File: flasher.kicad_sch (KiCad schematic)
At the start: 22 parts, among them Q2 SS8050_C2150, Q3 SS8050_C2150, U5 CH343G

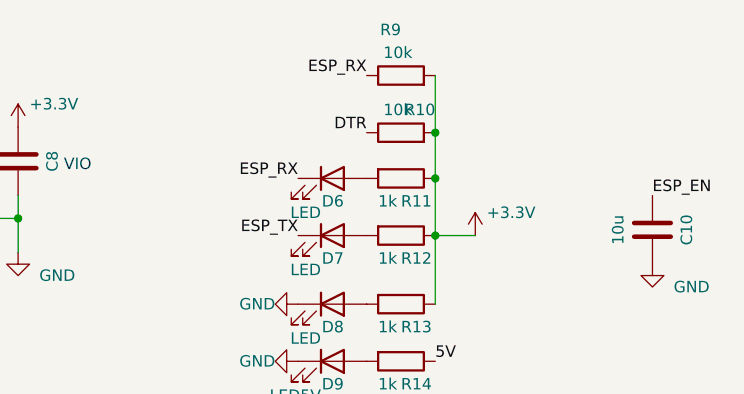
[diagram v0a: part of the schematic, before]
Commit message: changed footprints
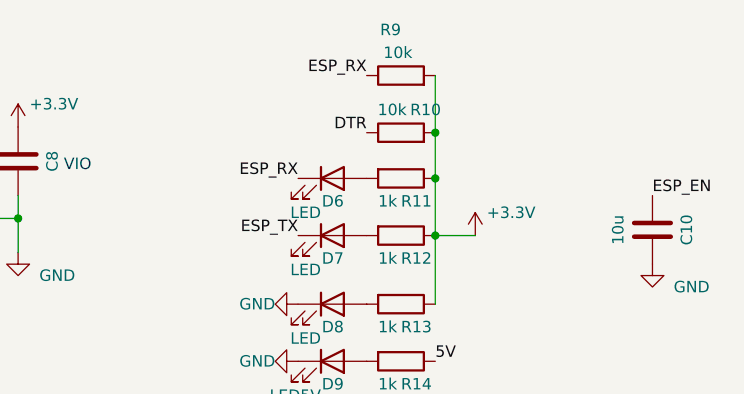
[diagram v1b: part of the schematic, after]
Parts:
- R10, R11, R12, R13, R14, R5, R6, R7, R8, R9: footprint Resistor_SMD:R_0402_1005Metric -> Resistor_SMD:R_1206_3216Metric
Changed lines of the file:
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@@
       (effects (font (size 1.27 1.27)) (justify left))
     )
-    (property "Footprint" "Resistor_SMD:R_0402_1005Metric" (at 132.715 38.862 90)
+    (property "Footprint" "Resistor_SMD:R_1206_3216Metric" (at 132.715 38.862 90)
       (effects (font (size 1.27 1.27)) hide)
     )
@@
       (effects (font (size 1.27 1.27)) (justify left))
     )
-    (property "Footprint" "Resistor_SMD:R_0402_1005Metric" (at 132.715 24.638 90)
+    (property "Footprint" "Resistor_SMD:R_1206_3216Metric" (at 132.715 24.638 90)
       (effects (font (size 1.27 1.27)) hide)
     )
@@
       (effects (font (size 1.27 1.27)) (justify left))
     )
-    (property "Footprint" "Resistor_SMD:R_0402_1005Metric" (at 132.715 46.482 90)
+    (property "Footprint" "Resistor_SMD:R_1206_3216Metric" (at 132.715 46.482 90)
       (effects (font (size 1.27 1.27)) hide)
     )
@@
   (symbol (lib_id "Device:R") (at 132.715 29.21 90) (unit 1)
     (in_bom yes) (on_board yes) (dnp no)
-    (property "Reference" "R10" (at 136.525 26.67 90)
-      (effects (font (size 1.27 1.27)) (justify left))
-    )
-    (property "Value" "10k" (at 133.985 26.67 90)
-      (effects (font (size 1.27 1.27)) (justify left))
-    )
-    (property "Footprint" "Resistor_SMD:R_0402_1005Metric" (at 132.715 30.988 90)
+    (property "Reference" "R10" (at 137.16 26.67 90)
+      (effects (font (size 1.27 1.27)) (justify left))
+    )
+    (property "Value" "10k" (at 133.35 26.67 90)
+      (effects (font (size 1.27 1.27)) (justify left))
+    )
+    (property "Footprint" "Resistor_SMD:R_1206_3216Metric" (at 132.715 30.988 90)
       (effects (font (size 1.27 1.27)) hide)
     )
@@
       (effects (font (size 1.27 1.27)) (justify left))
     )
-    (property "Footprint" "Resistor_SMD:R_0402_1005Metric" (at 29.21 39.878 90)
+    (property "Footprint" "Resistor_SMD:R_1206_3216Metric" (at 29.21 39.878 90)
       (effects (font (size 1.27 1.27)) hide)
     )
@@
       (effects (font (size 1.27 1.27)) (justify left))
     )
-    (property "Footprint" "Resistor_SMD:R_0402_1005Metric" (at 29.21 25.908 90)
+    (property "Footprint" "Resistor_SMD:R_1206_3216Metric" (at 29.21 25.908 90)
       (effects (font (size 1.27 1.27)) hide)
     )
@@
       (effects (font (size 1.27 1.27)) (justify left))
     )
-    (property "Footprint" "Resistor_SMD:R_0402_1005Metric" (at 132.715 32.512 90)
+    (property "Footprint" "Resistor_SMD:R_1206_3216Metric" (at 132.715 32.512 90)
       (effects (font (size 1.27 1.27)) hide)
     )
@@
       (effects (font (size 1.27 1.27)) (justify left))
     )
-    (property "Footprint" "Resistor_SMD:R_0402_1005Metric" (at 39.37 87.757 90)
+    (property "Footprint" "Resistor_SMD:R_1206_3216Metric" (at 39.37 87.757 90)
       (effects (font (size 1.27 1.27)) hide)
     )
@@
       (effects (font (size 1.27 1.27)) (justify left))
     )
-    (property "Footprint" "Resistor_SMD:R_0402_1005Metric" (at 72.39 87.757 90)
+    (property "Footprint" "Resistor_SMD:R_1206_3216Metric" (at 72.39 87.757 90)
       (effects (font (size 1.27 1.27)) hide)
     )
@@
       (effects (font (size 1.27 1.27)) (justify left))
     )
-    (property "Footprint" "Resistor_SMD:R_0402_1005Metric" (at 132.715 52.832 90)
-      (effects (font (size 1.27 1.27)) hide)
-    )
+    (property "Footprint" "Resistor_SMD:R_1206_3216Metric" (at 132.715 52.832 90)
+      (effects (font (size 1.27 1.27)) hide)
+    )

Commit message: Weniger schwerbehinderte grid koordinaten
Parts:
- added NT101: NetTie_3, NetTie:NetTie-3_SMD_Pad0.5mm, symbol Device:NetTie_3
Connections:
- net +5V: now also NT101.2; no longer USBC1.A4-B9 (VBUS), USBC1.B4-A9 (VBUS)
- new net THIN_USB_FLASHER_0: NT101.1, USBC1.A4-B9 (VBUS)
- new net THIN_USB_FLASHER_1: NT101.3, USBC1.B4-A9 (VBUS)
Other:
- moved on the sheet: C10, C7, C8, C9, D6, D7, D8, D9, Q2, Q3, R10, R11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

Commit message: everything changed once again
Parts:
- C10, C8: footprint Capacitor_SMD:C_0603_1608Metric -> Capacitor_SMD:C_1206_3216Metric
- C7, C9: footprint Capacitor_SMD:C_0402_1005Metric -> Capacitor_SMD:C_1206_3216Metric
- D9: value LED5V -> LED

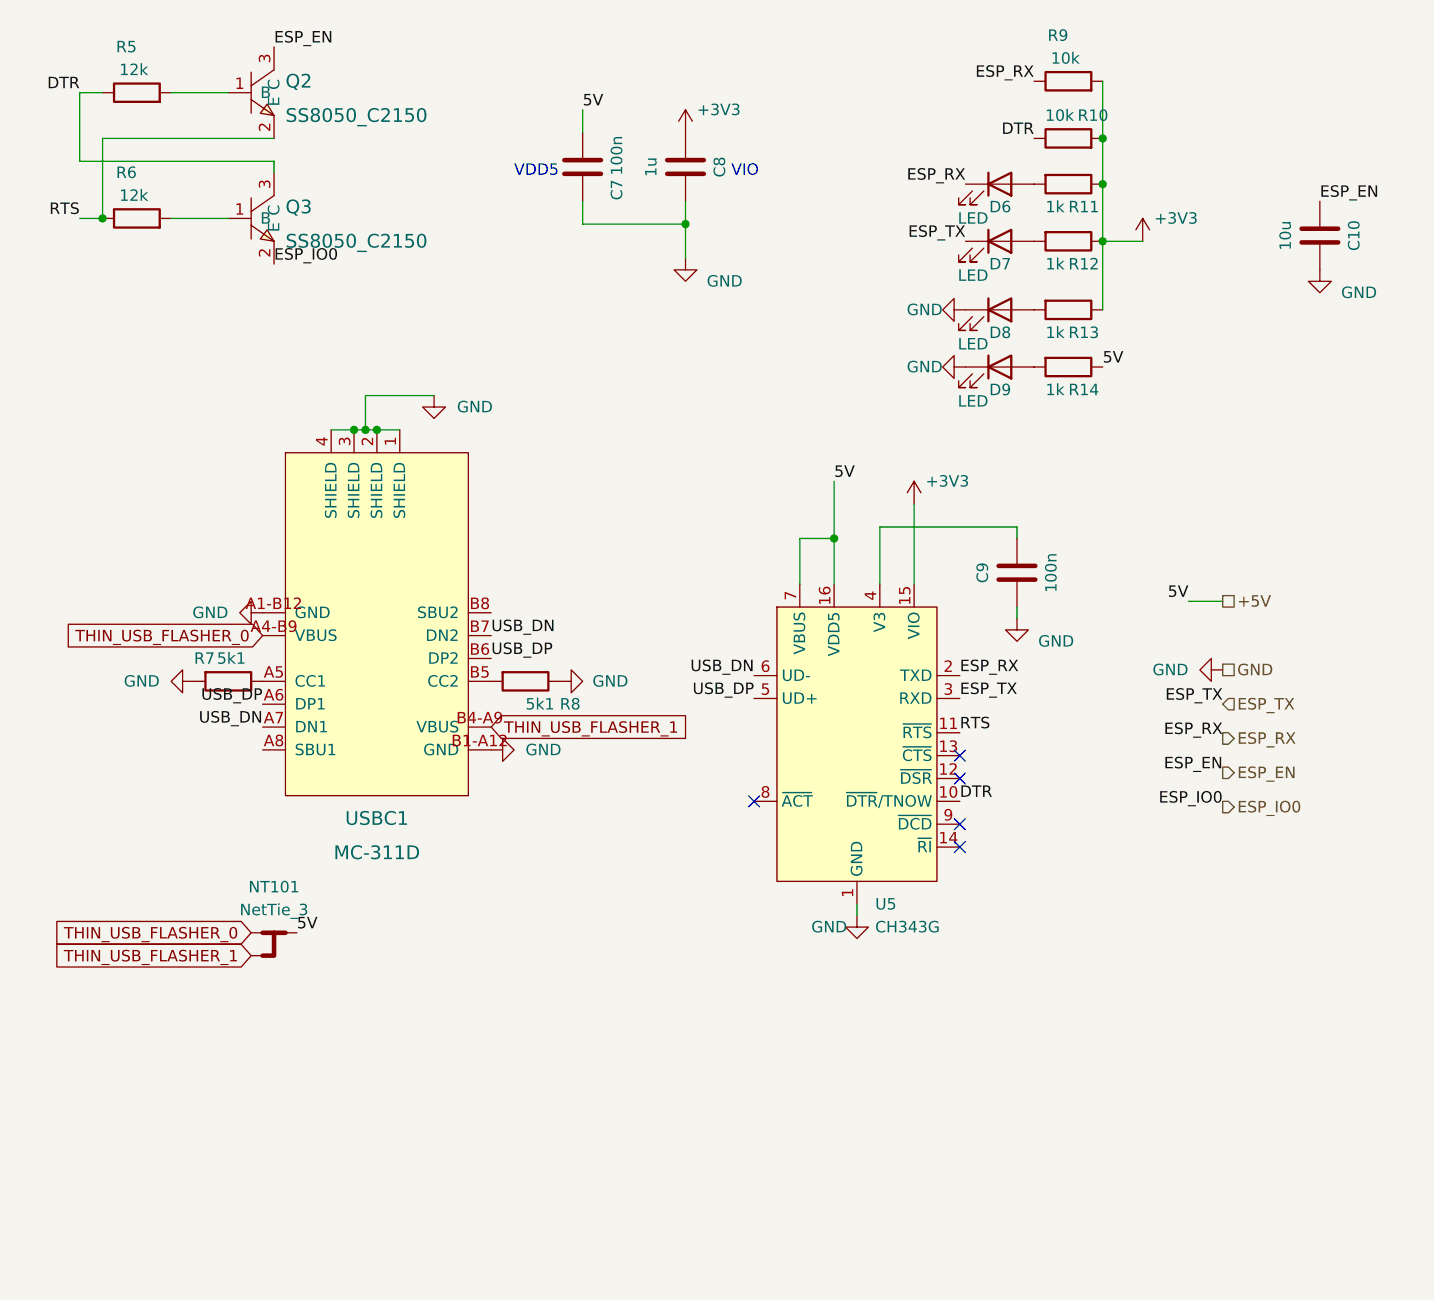
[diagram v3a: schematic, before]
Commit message: Dont use global net labels
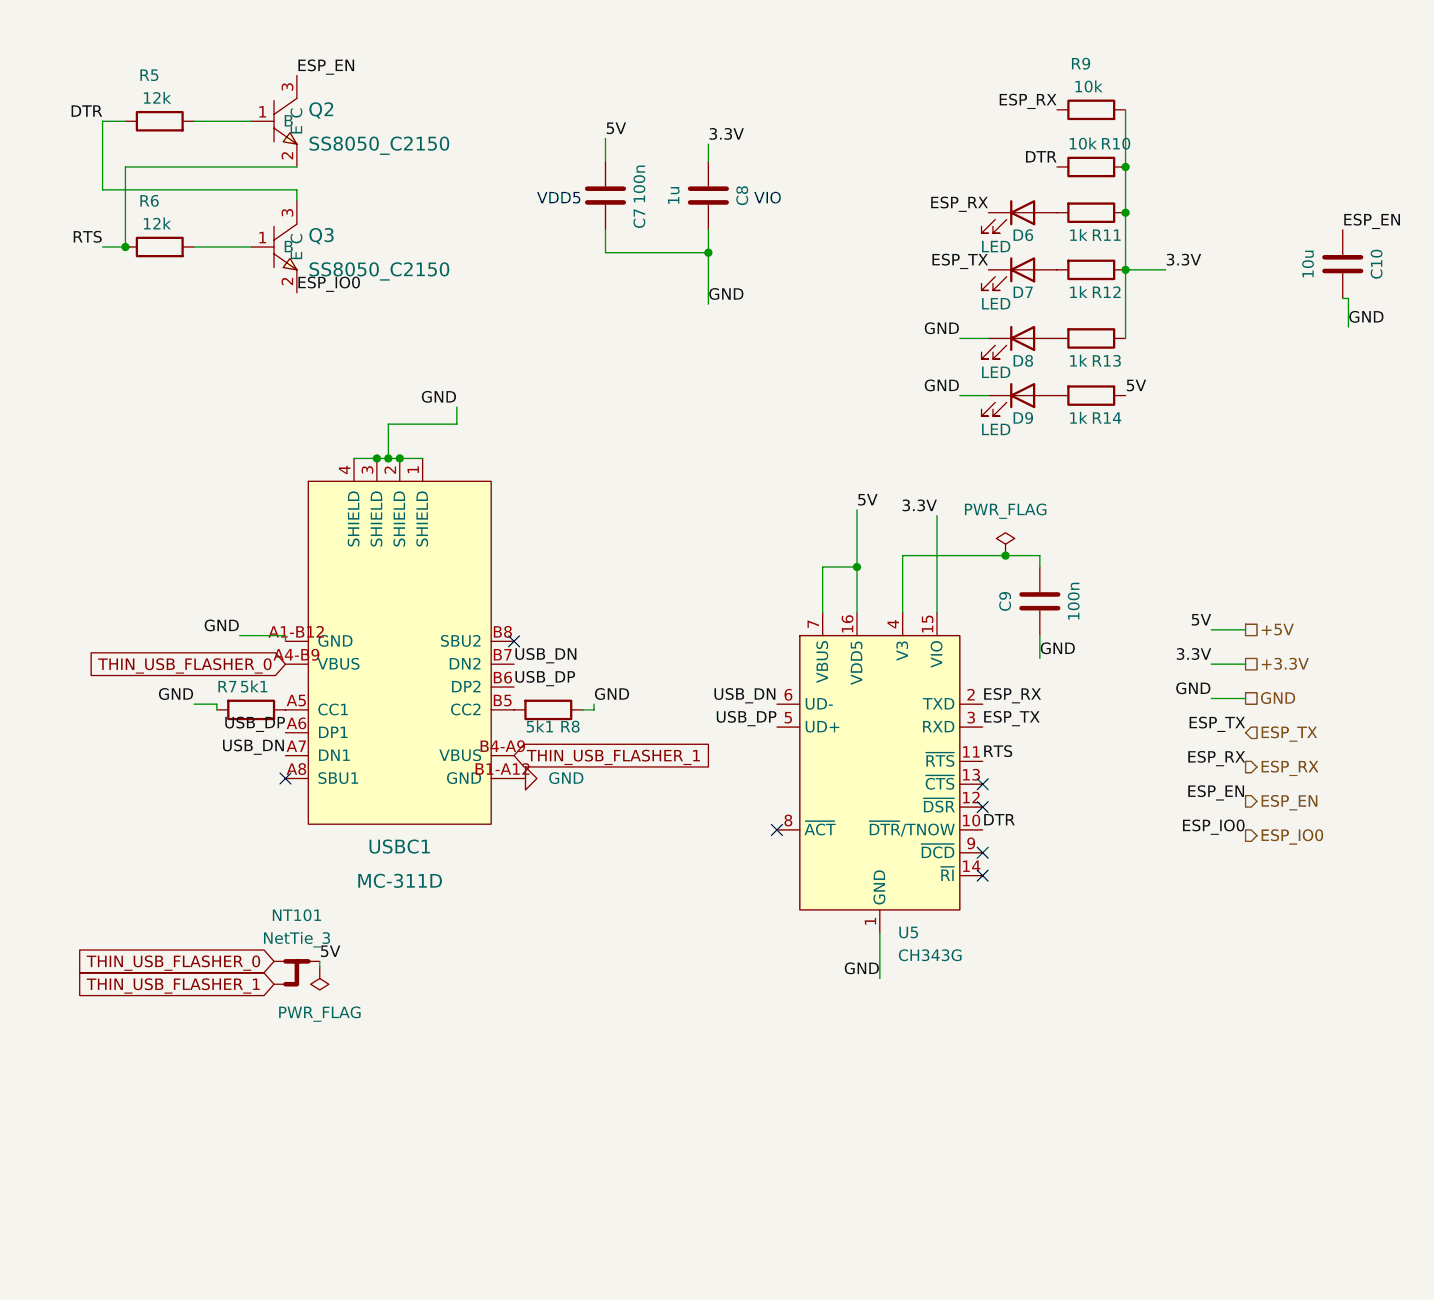
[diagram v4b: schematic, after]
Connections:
- net +3V3 renamed +3.3V
- no-connect marks 5 -> 7
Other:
- moved on the sheet: C10, C7, C8, C9, D6, D7, D8, D9, NT101, Q2, Q3, R10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

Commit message: Update flasher
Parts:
- removed C10: 10u, Capacitor_SMD:C_1206_3216Metric, symbol Device:C
- C7, C9: Field-1 (none) -> ${DNP}; LCSC Part # C1525 -> C24497
- C8, D6, D7, D8, D9, NT101, Q2, Q3, R10, R11, R12, R13, R14, R5, R6, R7, R8, R9, U5, USBC1: Field-1 (none) -> ${DNP}
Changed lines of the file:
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@@
-    (stroke (width 0) (type default))
-  )
-  (wire (pts (xy 163.83 50.8) (xy 163.83 47.625))
     (stroke (width 0) (type default))
   )
@@
   )
   (wire (pts (xy 46.99 33.02) (xy 27.94 33.02))
-    (stroke (width 0) (type default))
-  )
-  (wire (pts (xy 163.83 47.625) (xy 163.195 47.625))
     (stroke (width 0) (type default))
   )
@@
     (effects (font (size 1.27 1.27)) (justify right bottom))
   )
-  (label "GND" (at 163.83 50.8 0) (fields_autoplaced)
-    (effects (font (size 1.27 1.27)) (justify left bottom))
-  )
   (label "ESP_IO0" (at 46.99 46.99 0) (fields_autoplaced)
     (effects (font (size 1.27 1.27)) (justify left bottom))
@@
   )
   (label "3.3V" (at 143.51 44.45 0) (fields_autoplaced)
-    (effects (font (size 1.27 1.27)) (justify left bottom))
-  )
-  (label "ESP_EN" (at 163.195 40.005 0) (fields_autoplaced)
     (effects (font (size 1.27 1.27)) (justify left bottom))
   )
@@
       (effects (font (size 1.27 1.27)) hide)
     )
+    (property "Field-1" "${DNP}" (at 135.255 44.45 0)
+      (effects (font (size 1.27 1.27)) hide)
+    )
+    (property "Field-1" "${DNP}" (at 135.255 44.45 0)
+      (effects (font (size 1.27 1.27)) hide)
+    )
     (pin "1")
     (pin "2")
@@
       (effects (font (size 1.27 1.27)) hide)
     )
+    (property "Field-1" "${DNP}" (at 127.635 52.07 0)
+      (effects (font (size 1.27 1.27)) hide)
+    )
+    (property "Field-1" "${DNP}" (at 127.635 52.07 0)
+      (effects (font (size 1.27 1.27)) hide)
+    )
     (pin "1")
     (pin "2")
@@
     )
   )
-  (symbol (lib_id "Device:C") (at 163.195 43.815 180) (unit 1)
-    (in_bom yes) (on_board yes) (dnp no)
-    (property "Reference" "C10" (at 167.005 43.815 90)
-      (effects (font (size 1.27 1.27)))
-    )
-    (property "Value" "10u" (at 159.385 43.815 90)
-      (effects (font (size 1.27 1.27)))
-    )
-    (property "Footprint" "Capacitor_SMD:C_1206_3216Metric" (at 162.2298 40.005 0)
-      (effects (font (size 1.27 1.27)) hide)
-    )
-    (property "Datasheet" "~" (at 163.195 43.815 0)
-      (effects (font (size 1.27 1.27)) hide)
-    )
-    (property "Description" "Unpolarized capacitor" (at 163.195 43.815 0)
-      (effects (font (size 1.27 1.27)) hide)
-    )
-    (property "LCSC Part #" "C96446" (at 163.195 43.815 90)
-      (effects (font (size 1.27 1.27)) hide)
-    )
-    (pin "1")
-    (pin "2")
-    (instances
-      (project "esp32_midi"
-        (path "/e33c0603-5c0d-4712-ab63-5756d1504b4c/2c215fe4-7c9a-4ae0-9a5d-913b04975b72"
-          (reference "C10") (unit 1)
-        )
-      )
-    )
-  )
   (symbol (lib_id "Device:R") (at 135.255 26.67 90) (unit 1)
     (in_bom yes) (on_board yes) (dnp no)
@@
     )
     (property "LCSC Part #" "C25744" (at 135.255 26.67 0)
+      (effects (font (size 1.27 1.27)) hide)
+    )
+    (property "Field-1" "${DNP}" (at 135.255 26.67 0)
+      (effects (font (size 1.27 1.27)) hide)
+    )
+    (property "Field-1" "${DNP}" (at 135.255 26.67 0)
       (effects (font (size 1.27 1.27)) hide)
     )
@@
       (effects (font (size 1.27 1.27)) hide)
     )
+    (property "Field-1" "${DNP}" (at 127.635 58.42 0)
+      (effects (font (size 1.27 1.27)) hide)
+    )
+    (property "Field-1" "${DNP}" (at 127.635 58.42 0)
+      (effects (font (size 1.27 1.27)) hide)
+    )
     (pin "1")
     (pin "2")
@@
       (effects (font (size 1.27 1.27)) hide)
     )
+    (property "Field-1" "${DNP}" (at 127.635 44.45 0)
+      (effects (font (size 1.27 1.27)) hide)
+    )
+    (property "Field-1" "${DNP}" (at 127.635 44.45 0)
+      (effects (font (size 1.27 1.27)) hide)
+    )
     (pin "1")
     (pin "2")
@@
     )
     (property "LCSC Part #" "C11702" (at 135.255 52.07 0)
+      (effects (font (size 1.27 1.27)) hide)
+    )
+    (property "Field-1" "${DNP}" (at 135.255 52.07 0)
+      (effects (font (size 1.27 1.27)) hide)
+    )
+    (property "Field-1" "${DNP}" (at 135.255 52.07 0)
       (effects (font (size 1.27 1.27)) hide)
     )
@@
       (effects (font (size 1.27 1.27)) hide)
     )
+    (property "Field-1" "${DNP}" (at 92.71 36.195 0)
+      (effects (font (size 1.27 1.27)) hide)
+    )
+    (property "Field-1" "${DNP}" (at 92.71 36.195 0)
+      (effects (font (size 1.27 1.27)) hide)
+    )
     (pin "1")
     (pin "2")
@@
       (effects (font (size 1.27 1.27)) hide)
     )
+    (property "Field-1" "${DNP}" (at 135.255 33.02 0)
+      (effects (font (size 1.27 1.27)) hide)
+    )
+    (property "Field-1" "${DNP}" (at 135.255 33.02 0)
+      (effects (font (size 1.27 1.27)) hide)
+    )
     (pin "1")
     (pin "2")
@@
       (effects (font (size 1.27 1.27)) hide)
     )
+    (property "Field-1" "${DNP}" (at 31.75 41.91 0)
+      (effects (font (size 1.27 1.27)) hide)
+    )
+    (property "Field-1" "${DNP}" (at 31.75 41.91 0)
+      (effects (font (size 1.27 1.27)) hide)
+    )
     (pin "1")
     (pin "2")
@@
       (effects (font (size 1.27 1.27)) hide)
     )
+    (property "Field-1" "${DNP}" (at 31.75 27.94 0)
+      (effects (font (size 1.27 1.27)) hide)
+    )
+    (property "Field-1" "${DNP}" (at 31.75 27.94 0)
+      (effects (font (size 1.27 1.27)) hide)
+    )
     (pin "1")
     (pin "2")
@@
       (effects (font (size 1.27 1.27)) hide)
     )
+    (property "Field-1" "${DNP}" (at 135.255 38.1 0)
+      (effects (font (size 1.27 1.27)) hide)
+    )
+    (property "Field-1" "${DNP}" (at 135.255 38.1 0)
+      (effects (font (size 1.27 1.27)) hide)
+    )
     (pin "1")
     (pin "2")
@@
     )
     (property "LCSC Part #" "C25905" (at 41.91 93.345 0)
+      (effects (font (size 1.27 1.27)) hide)
+    )
+    (property "Field-1" "${DNP}" (at 41.91 93.345 0)
+      (effects (font (size 1.27 1.27)) hide)
+    )
+    (property "Field-1" "${DNP}" (at 41.91 93.345 0)
       (effects (font (size 1.27 1.27)) hide)
     )
@@
       (effects (font (size 1.27 1.27)) hide)
     )
+    (property "Field-1" "${DNP}" (at 46.99 41.91 0)
+      (effects (font (size 1.27 1.27)) hide)
+    )
+    (property "Field-1" "${DNP}" (at 46.99 41.91 0)
+      (effects (font (size 1.27 1.27)) hide)
+    )
     (pin "1")
     (pin "2")
@@
       (effects (font (size 1.27 1.27)) hide)
     )
+    (property "Field-1" "${DNP}" (at 127.635 38.1 0)
+      (effects (font (size 1.27 1.27)) hide)
+    )
+    (property "Field-1" "${DNP}" (at 127.635 38.1 0)
+      (effects (font (size 1.27 1.27)) hide)
+    )
     (pin "1")
     (pin "2")
@@
       (effects (font (size 1.27 1.27)) hide)
     )
-    (property "LCSC Part #" "C1525" (at 129.54 81.28 90)
+    (property "LCSC Part #" "C24497" (at 129.54 81.28 90)
+      (effects (font (size 1.27 1.27)) hide)
+    )
+    (property "Field-1" "${DNP}" (at 129.54 81.28 0)
+      (effects (font (size 1.27 1.27)) hide)
+    )
+    (property "Field-1" "${DNP}" (at 129.54 81.28 0)
       (effects (font (size 1.27 1.27)) hide)
     )
@@
     )
     (property "LCSC Part #" "C136423" (at 58.42 84.455 0)
+      (effects (font (size 1.27 1.27)) hide)
+    )
+    (property "Field-1" "${DNP}" (at 58.42 84.455 0)
+      (effects (font (size 1.27 1.27)) hide)
+    )
+    (property "Field-1" "${DNP}" (at 58.42 84.455 0)
       (effects (font (size 1.27 1.27)) hide)
     )
@@
       (effects (font (size 1.27 1.27)) hide)
     )
+    (property "Field-1" "${DNP}" (at 74.93 93.345 0)
+      (effects (font (size 1.27 1.27)) hide)
+    )
+    (property "Field-1" "${DNP}" (at 74.93 93.345 0)
+      (effects (font (size 1.27 1.27)) hide)
+    )
     (pin "1")
     (pin "2")
@@
       (effects (font (size 1.27 1.27)) hide)
     )
+    (property "Field-1" "${DNP}" (at 46.99 27.94 0)
+      (effects (font (size 1.27 1.27)) hide)
+    )
+    (property "Field-1" "${DNP}" (at 46.99 27.94 0)
+      (effects (font (size 1.27 1.27)) hide)
+    )
     (pin "1")
     (pin "2")
@@
     )
     (property "LCSC Part #" "C2844153" (at 111.76 100.33 0)
+      (effects (font (size 1.27 1.27)) hide)
+    )
+    (property "Field-1" "${DNP}" (at 111.76 100.33 0)
+      (effects (font (size 1.27 1.27)) hide)
+    )
+    (property "Field-1" "${DNP}" (at 111.76 100.33 0)
       (effects (font (size 1.27 1.27)) hide)
     )
@@
       (effects (font (size 1.27 1.27)) hide)
     )
+    (property "Field-1" "${DNP}" (at 135.255 58.42 0)
+      (effects (font (size 1.27 1.27)) hide)
+    )
+    (property "Field-1" "${DNP}" (at 135.255 58.42 0)
+      (effects (font (size 1.27 1.27)) hide)
+    )
     (pin "1")
     (pin "2")
@@
       (effects (font (size 1.27 1.27)) hide)
     )
+    (property "Field-1" "${DNP}" (at 46.99 121.285 0)
+      (effects (font (size 1.27 1.27)) hide)
+    )
+    (property "Field-1" "${DNP}" (at 46.99 121.285 0)
+      (effects (font (size 1.27 1.27)) hide)
+    )
     (pin "1")
     (pin "2")
@@
       (effects (font (size 1.27 1.27)) hide)
     )
-    (property "LCSC Part #" "C1525" (at 81.28 36.195 90)
-      (effects (font (size 1.27 1.27)) hide)
-    )
+    (property "LCSC Part #" "C24497" (at 81.28 36.195 90)
+      (effects (font (size 1.27 1.27)) hide)
+    )
+    (property "Field-1" "${DNP}" (at 81.28 36.195 0)
+      (effects (font (size 1.27 1.27)) hide)
+    )
+    (property "Field-1" "${DNP}" (at 81.28 36.195 0)
+      (effects (font (size 1.27 1.27)) hide)
+    )
